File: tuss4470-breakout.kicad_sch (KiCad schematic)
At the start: 17 parts, among them J1 Conn_01x02_Socket, U1 TUSS4470, U2 LP5907MFX-3.3

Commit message: add gitignore, continue schematic
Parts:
- added J2: Conn_01x02_Pin, symbol Connector:Conn_01x02_Pin
- added J3: Conn_01x12_Pin, symbol Connector:Conn_01x12_Pin
- C4: value C_Small -> 16n
- C5: value C_Small -> 100n
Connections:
- net CS: now also J3.6 (Pin_6)
- net DGND: now also J2.2 (Pin_2)
- net GND: now also J3.12 (Pin_12), J3.2 (Pin_2)
- net IO1: now also J3.7 (Pin_7)
- net IO2: now also J3.8 (Pin_8)
- net OUT3: now also J3.9 (Pin_9)
- net OUT4: now also J3.10 (Pin_10)
- net SCLK: now also J3.3 (Pin_3)
- net SDI: now also J3.4 (Pin_4)
- net SDO: now also J3.5 (Pin_5)
- net VIN: now also J2.1 (Pin_1)
- net VLDO: now also J3.1 (Pin_1)
- net VOUT: now also J3.11 (Pin_11)
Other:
- note added: "C_{FLT} = 25/(2·π·6250·f_{DRV_CLK}) mit DRV_CLK = 40kHz -> 15.9 nF"
- note added: "C_{INN} = 1/(2·π·150·(f_{DRV_CLK}/4)) mit DRV_CLK = 40kHz -> 106 nF"
- note removed: "C_{FLT} = 25/(2·π·6250·f_{DRV_CLK})"
- note removed: "C_{INN} = 1/(2·π·150·(f_{DRV_CLK}/4))"
- moved on the sheet: C1, C2, C3, C4, C5, C6, D1, J1, R1, R2, U1

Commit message: layout finished
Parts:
- removed J1: Conn_01x02_Socket, symbol Connector:Conn_01x02_Socket
- removed J2: Conn_01x02_Pin, symbol Connector:Conn_01x02_Pin
- removed J3: Conn_01x12_Pin, symbol Connector:Conn_01x12_Pin
- added H1, H2: MountingHole, MountingHole:MountingHole_3.2mm_M3, symbol Mechanical:MountingHole
- added J1, J4: Screw_Terminal_01x02, TerminalBlock:TerminalBlock_Xinya_XY308-2.54-2P_1x02_P2.54mm_Horizontal, symbol Connector:Screw_Terminal_01x02
- added J2, J3: Conn_01x08_Pin, Connector_PinHeader_2.54mm:PinHeader_1x08_P2.54mm_Vertical, symbol Connector:Conn_01x08_Pin
- added JP1: VPWR SEL, Connector_PinHeader_2.54mm:PinHeader_1x03_P2.54mm_Vertical, symbol Jumper:Jumper_3_Open
- C1: renamed from C8; footprint (none) -> Capacitor_SMD:C_0603_1608Metric
- C2: renamed from C7; footprint (none) -> Capacitor_SMD:C_0603_1608Metric
- C3: renamed from C1; footprint (none) -> Capacitor_SMD:C_0603_1608Metric
- C4: renamed from C3; footprint (none) -> Capacitor_SMD:C_0603_1608Metric
- C5: renamed from C2; footprint (none) -> Capacitor_SMD:C_0603_1608Metric
- C6: footprint (none) -> Capacitor_SMD:C_0603_1608Metric
- C7: renamed from C4; footprint (none) -> Capacitor_SMD:C_0603_1608Metric
- C8: renamed from C5; footprint (none) -> Capacitor_SMD:C_0603_1608Metric
- D1: footprint (none) -> Diode_SMD:D_SOD-123
- R1: renamed from R5; footprint (none) -> Resistor_SMD:R_0603_1608Metric
- R2: renamed from R3; footprint (none) -> Resistor_SMD:R_0603_1608Metric
- R3: renamed from R4; footprint (none) -> Resistor_SMD:R_0603_1608Metric
- R4: renamed from R2; footprint (none) -> Resistor_SMD:R_0603_1608Metric
- R5: renamed from R1; footprint (none) -> Resistor_SMD:R_0603_1608Metric
- renumbered U2 to U1, U1 to U2
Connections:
- net GND is gone; now on net DGND: C1.2, C2.2, C4.2, C7.2, C8.2, U1.2 (GND), U2.13 (SGND), U2.14 (GND), U2.21 (EPAD)
- net CS: now also J2.3 (Pin_3)
- net DGND: now also J1.2 (Pin_2), J2.8 (Pin_8), J3.8 (Pin_8)
- net IO1: now also J2.2 (Pin_2)
- net IO2: now also J3.1 (Pin_1)
- net OUT3: now also J3.3 (Pin_3)
- net OUT4: now also J3.2 (Pin_2)
- net SCLK: now also J2.4 (Pin_4)
- net SDI: now also J2.6 (Pin_6)
- net SDO: now also J2.5 (Pin_5)
- net VOUT: now also J2.1 (Pin_1)
- net at R5.1, U2.15 (OUTA): now also J4.1 (Pin_1)
- net at U2.16 (OUTB): now also J4.2 (Pin_2)
- net VIN renamed VPWR
- net VPWR: now also JP1.2 (C)
- net VLDO renamed 3V3
- net 3V3: now also J2.7 (Pin_7); no longer R1.1
- new net 5V: J3.7 (Pin_7), JP1.1 (A), R1.1
- new net VEXT: J1.1 (Pin_1), JP1.3 (B)
- no-connect marks 0 -> 3
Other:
- note added: "mikroBUS"
- moved on the sheet: C3, C4, C5, C6, C7, C8, D1, R4, R5, U2

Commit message: generate gerbers
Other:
- company: (none) -> Maximilian Weber
- title: (none) -> TUSS4470 Breakout Board
- moved on the sheet: C1, C2, C3, C4, C5, C6, C7, C8, D1, H1, H2, J1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

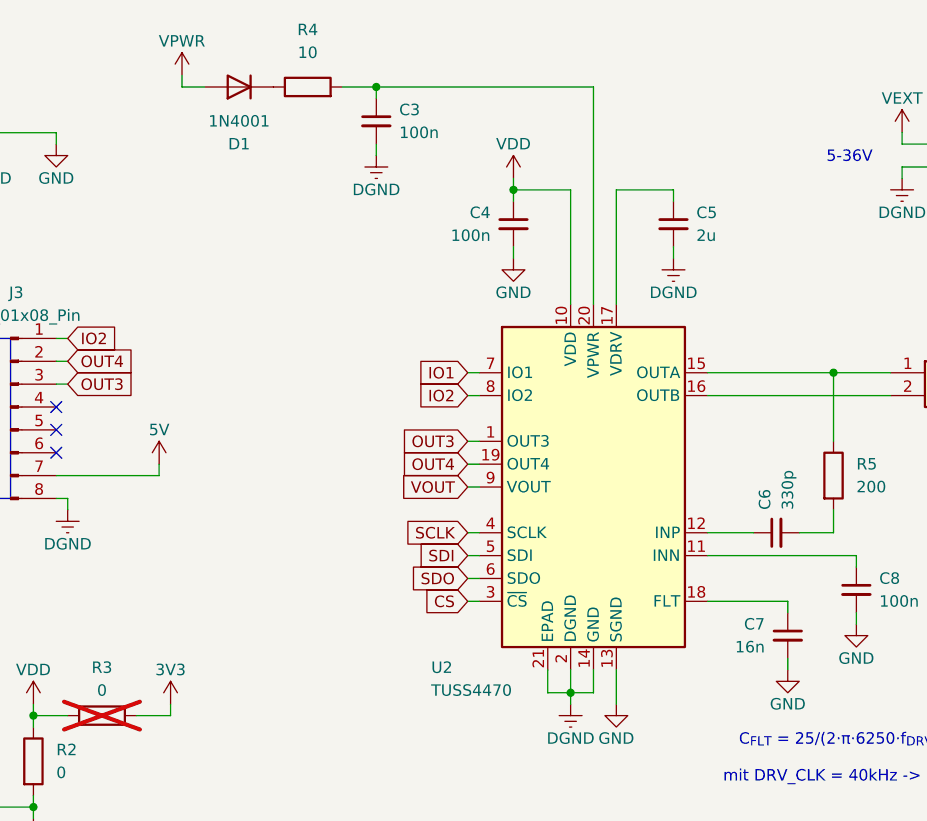
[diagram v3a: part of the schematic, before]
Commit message: v0.1 ordered pcb and components
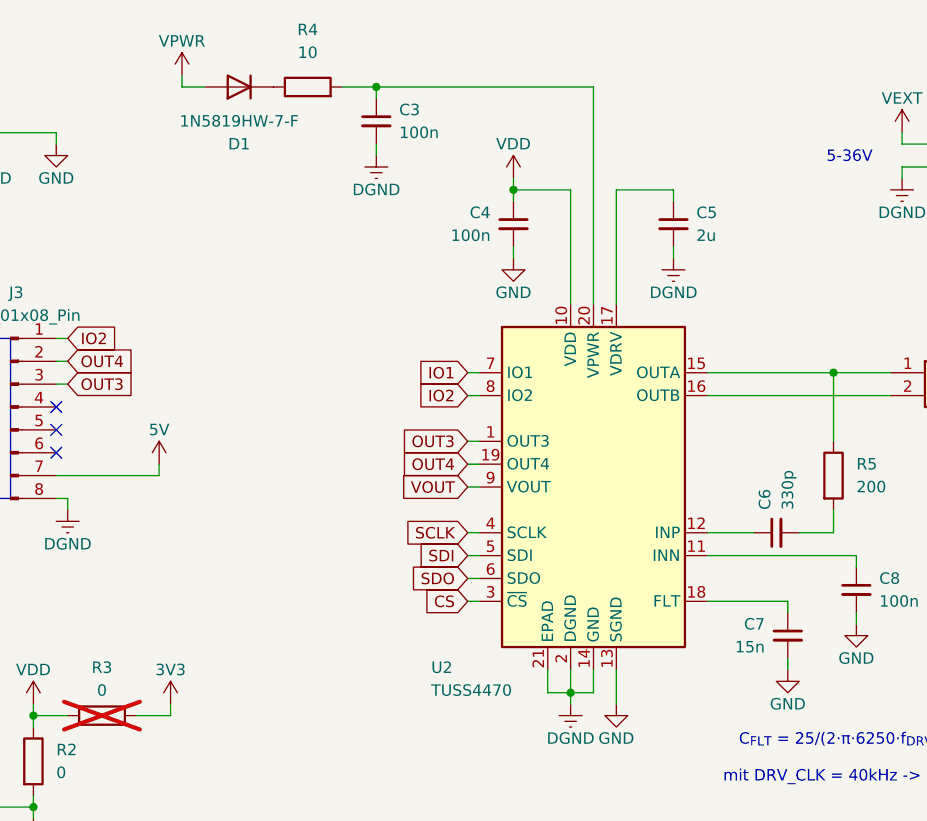
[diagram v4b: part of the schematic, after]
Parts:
- C1, C2, C5: LCSC Part (none) -> C913904
- C3, C4, C8: LCSC Part (none) -> C14663
- C6: LCSC Part (none) -> C1664
- C7: value 16n -> 15n; LCSC Part (none) -> C519550
- D1: value 1N4001 -> 1N5819HW-7-F; LCSC Part (none) -> C82544
- J1, J4: LCSC Part (none) -> C557685
- J2, J3: now left out of the parts list
- R1, R2, R3: LCSC Part (none) -> C95177
- R4: footprint Resistor_SMD:R_0603_1608Metric -> Resistor_SMD:R_0805_2012Metric; LCSC Part (none) -> C441940
- R5: footprint Resistor_SMD:R_0603_1608Metric -> Resistor_SMD:R_0805_2012Metric; LCSC Part (none) -> C5972814
- U1: LCSC Part (none) -> C80670
- U2: LCSC Part (none) -> C1855776
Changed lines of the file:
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@@
 			)
 		)
+		(property "LCSC Part" "C557685"
+			(at 158.75 54.61 0)
+			(hide yes)
+			(show_name no)
+			(do_not_autoplace no)
+			(effects
+				(font
+					(size 1.27 1.27)
+				)
+			)
+		)
 		(pin "1"
 		)
@@
 			)
 		)
-		(property "Value" "1N4001"
+		(property "Value" "1N5819HW-7-F"
 			(at 81.28 26.67 0)
 			(show_name no)
@@
 			)
 		)
-		(property "LCSC Part" ""
+		(property "LCSC Part" "C82544"
 			(at 81.28 22.86 0)
 			(hide yes)
@@
 			)
 		)
-		(property "Value" "16n"
+		(property "Value" "15n"
 			(at 139.7 85.0962 0)
 			(show_name no)
@@
 			)
 		)
-		(property "LCSC Part" ""
+		(property "LCSC Part" "C519550"
 			(at 142.24 83.82 0)
 			(hide yes)
@@
 			)
 		)
-		(property "LCSC Part" ""
+		(property "LCSC Part" "C14663"
 			(at 149.86 78.74 0)
 			(hide yes)
@@
 			)
 		)
-		(property "LCSC Part" ""
+		(property "LCSC Part" "C14663"
 			(at 96.52 26.67 0)
 			(hide yes)
@@
 			)
 		)
-		(property "LCSC Part" ""
+		(property "LCSC Part" "C1855776"
 			(at 120.65 67.31 0)
 			(hide yes)
@@
 			)
 		)
-		(property "LCSC Part" ""
+		(property "LCSC Part" "C80670"
 			(at 45.72 105.41 0)
 			(hide yes)
@@
 			)
 		)
-		(property "LCSC Part" ""
+		(property "LCSC Part" "C95177"
 			(at 31.75 97.79 0)
 			(hide yes)
@@
 			)
 		)
-		(property "LCSC Part" ""
+		(property "LCSC Part" "C95177"
 			(at 66.04 92.71 90)
 			(hide yes)
@@
 			)
 		)
+		(property "LCSC Part" "C557685"
+			(at 166.37 29.21 0)
+			(hide yes)
+			(show_name no)
+			(do_not_autoplace no)
+			(effects
+				(font
+					(size 1.27 1.27)
+				)
+			)
+		)
 		(pin "1"
 		)
@@
 			)
 		)
-		(property "LCSC Part" ""
+		(property "LCSC Part" "C913904"
 			(at 129.54 38.1 0)
 			(hide yes)
@@
 		(body_style 1)
 		(exclude_from_sim no)
-		(in_bom yes)
+		(in_bom no)
 		(on_board yes)
 		(in_pos_files yes)
@@
 			)
 		)
-		(property "LCSC Part" ""
+		(property "LCSC Part" "C913904"
 			(at 31.75 106.68 0)
 			(hide yes)
@@
 			)
 		)
-		(property "Footprint" "Resistor_SMD:R_0603_1608Metric"
+		(property "Footprint" "Resistor_SMD:R_0805_2012Metric"
 			(at 88.9 24.638 90)
 			(hide yes)
@@
 			)
 		)
-		(property "LCSC Part" ""
+		(property "LCSC Part" "C441940"
 			(at 88.9 22.86 90)
 			(hide yes)
@@
 			)
 		)
-		(property "LCSC Part" ""
+		(property "LCSC Part" "C14663"
 			(at 111.76 38.1 0)
 			(hide yes)
@@
 			)
 		)
-		(property "LCSC Part" ""
+		(property "LCSC Part" "C913904"
 			(at 58.42 106.68 0)
 			(hide yes)
@@
 			)
 		)
-		(property "LCSC Part" ""
+		(property "LCSC Part" "C1664"
 			(at 140.97 72.39 0)
 			(hide yes)
@@
 		(body_style 1)
 		(exclude_from_sim no)
-		(in_bom yes)
+		(in_bom no)
 		(on_board yes)
 		(in_pos_files yes)
@@
 			)
 		)
-		(property "Footprint" "Resistor_SMD:R_0603_1608Metric"
+		(property "Footprint" "Resistor_SMD:R_0805_2012Metric"
 			(at 145.542 66.04 90)
 			(hide yes)
@@
 			)
 		)
-		(property "LCSC Part" ""
+		(property "LCSC Part" "C5972814"
 			(at 147.32 66.04 0)
 			(hide yes)
@@
 			)
 		)
-		(property "LCSC Part" ""
+		(property "LCSC Part" "C95177"
 			(at 58.42 97.79 0)
 			(hide yes)
